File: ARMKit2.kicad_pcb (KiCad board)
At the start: 2 copper layers, 40 parts, among them P1 CONN_01X06, P2 CONN_01X32, P3 CONN_01X32, P4 USB_B, SW1 SW_PUSH, SW2 SW_PUSH, U1 STM32F405RG, U2 LT1761, Y1 Crystal, Y2 Crystal

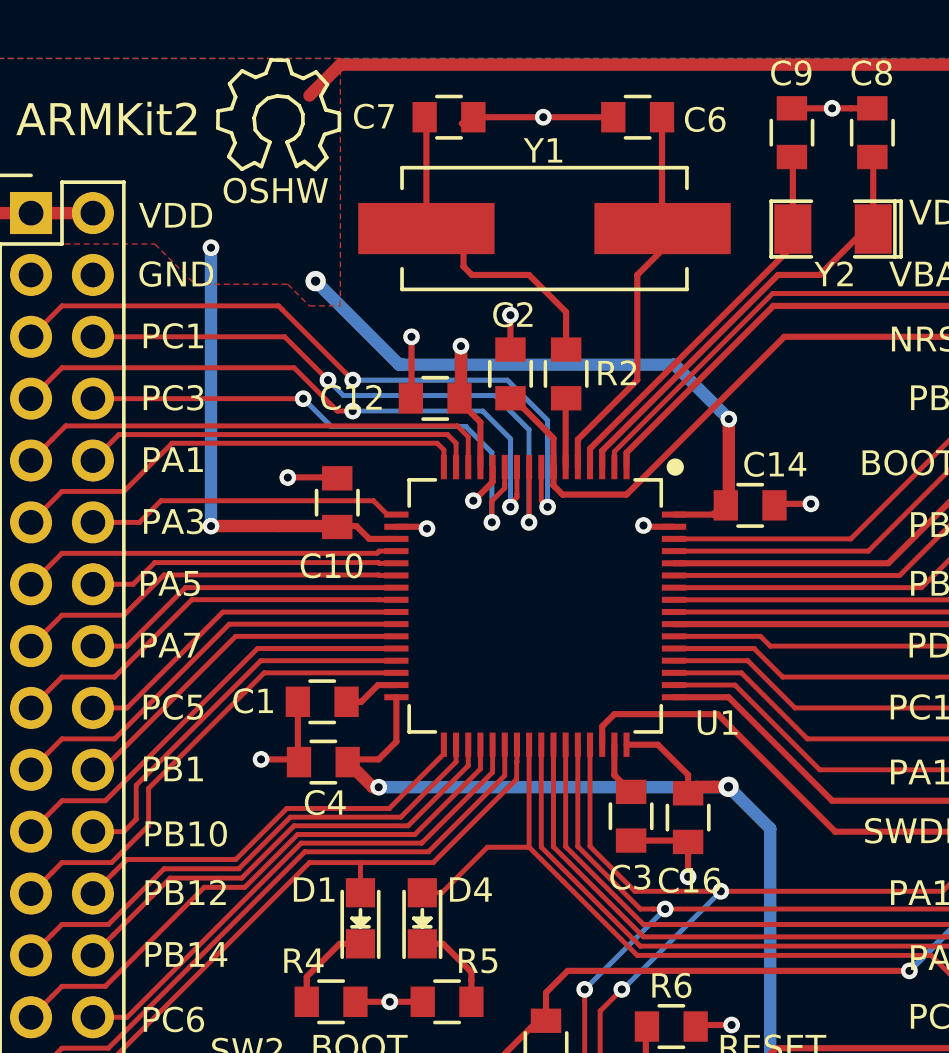
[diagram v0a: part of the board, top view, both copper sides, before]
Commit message: Updated for STM32F41x, STM32F4x1 compatibility
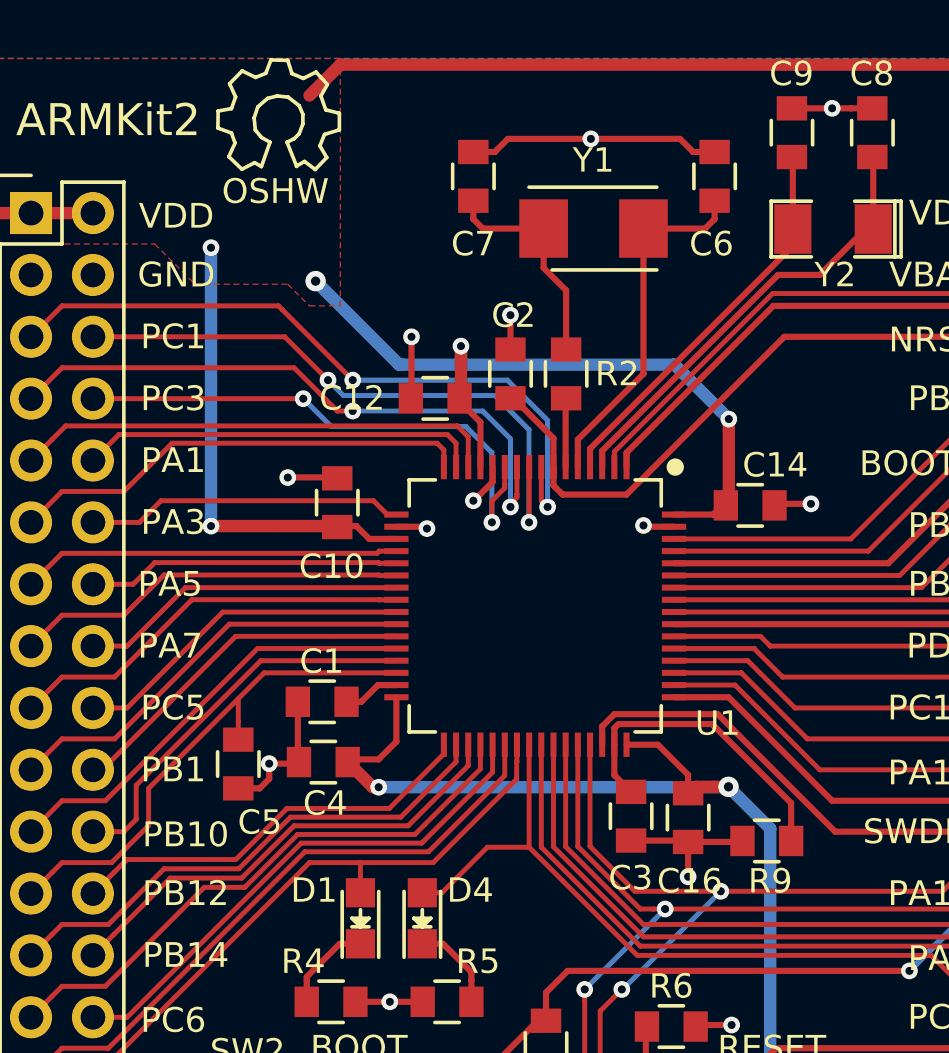
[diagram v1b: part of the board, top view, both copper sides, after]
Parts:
- added C5: 4.7uF, Capacitors_SMD:C_0805, F.Cu at (63.1, 111.5)
- added R9: DNP, Capacitors_SMD:C_0805, F.Cu at (84.8, 114.7)
- R7: value 10k -> 1k
- Y1: footprint Crystals:Crystal_HC49-SD_SMD -> Crystals:Crystal_SMD_5032_2Pads
- moved C6 3.98 mm to (82.7, 87.4), turned to 270 degrees
- moved C7 2.63 mm to (72.8, 87.4), turned to 270 degrees
- moved Y1 2.01 mm to (77.7, 89.5)
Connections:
- net PB11 renamed PB11/VCAP1
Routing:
- net VCAP2: track 2.22 -> 13.1 mm
- net GND: track 41.0 -> 49.5 mm
- net Net-(C7-Pad2): track 12.7 -> 9.52 mm
- net PB11/VCAP1: track 19.6 -> 21.3 mm
- net OSCIN: track 15.8 -> 14.7 mm

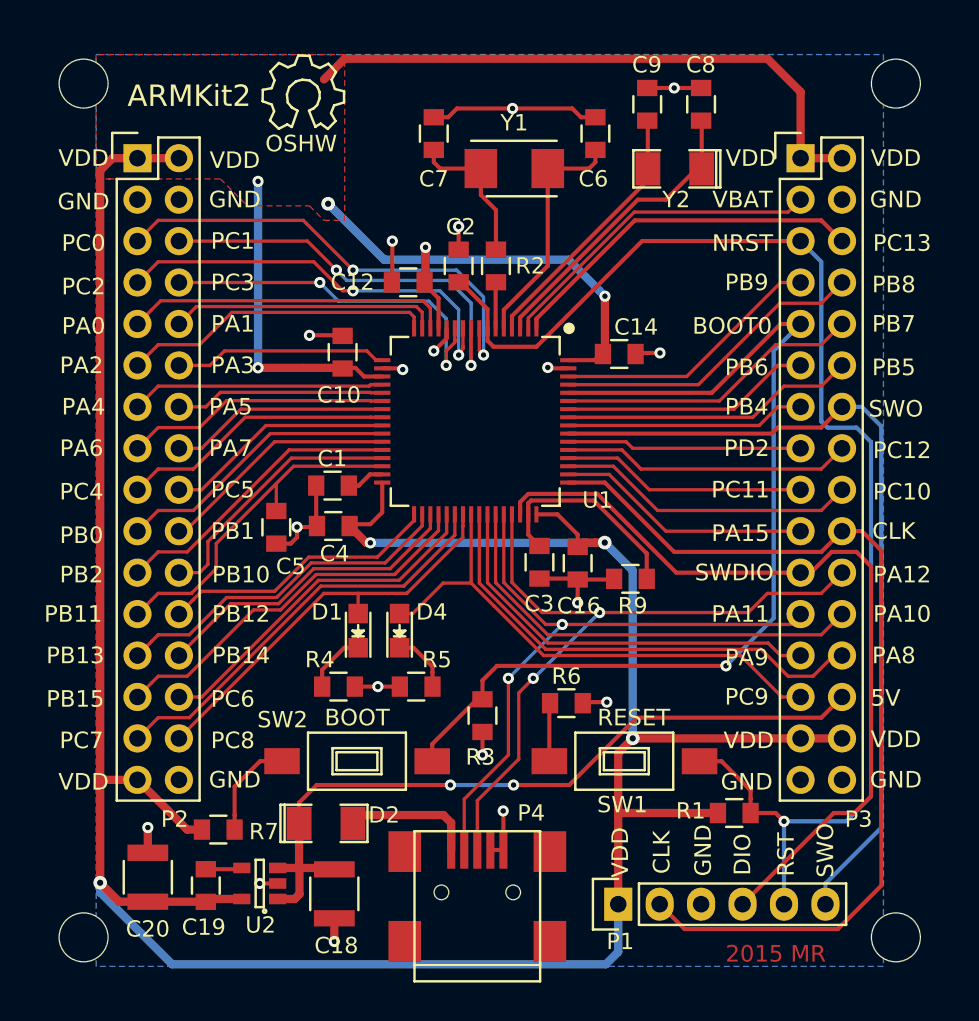
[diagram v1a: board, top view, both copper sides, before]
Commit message: Moved outline, can direct upload to OSHPark
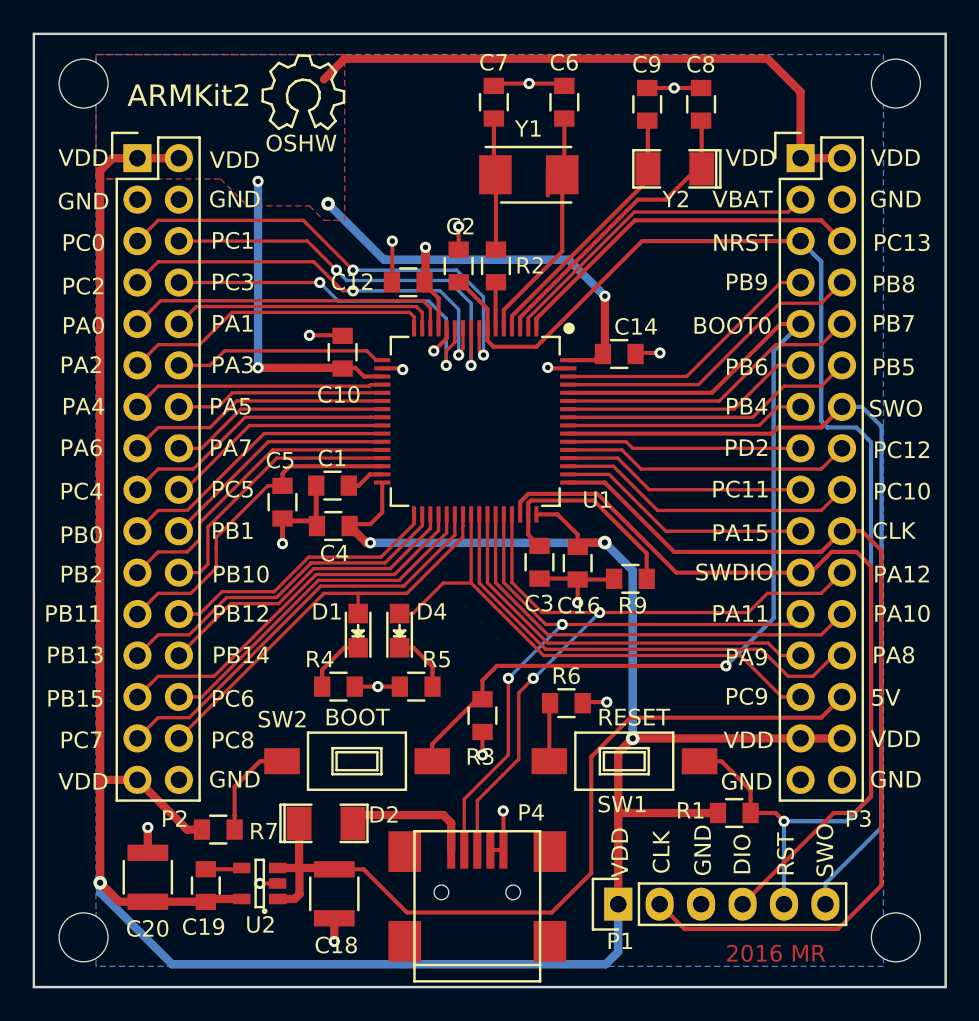
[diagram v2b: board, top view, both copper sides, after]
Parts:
- moved C7 4.15 mm to (76.5, 85.5)
- moved C6 2.71 mm to (80.8, 85.5)
- moved C5 1.59 mm to (63.5, 110.0)
- moved Y1 0.97 mm to (78.6, 89.9)
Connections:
- net PB11/VCAP1 renamed PB11_VCAP1
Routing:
- net GND: track 49.5 -> 43.7 mm
- net 5V_IN: track 46.5 -> 51.9 mm, vias 2 -> 0
- net Net-(C7-Pad2): track 9.52 -> 8.09 mm
- net OSCIN: track 14.7 -> 16.0 mm
- net PB11_VCAP1: track 21.3 -> 20.4 mm
- net PB2: track 18.1 -> 18.7 mm
- net PB10: track 16.2 -> 16.7 mm
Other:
- board outline added: 55.9 x 58.4 mm
- board text added: "2016 MR"
- board text removed: "2015 MR"
